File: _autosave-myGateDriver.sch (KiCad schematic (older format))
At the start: 99 parts, among them Q1 BC817, Q10 BC817, Q11 d44vh10, Q12 D45VH10, Q2 BC807, Q3 BC817, Q4 BC817, Q5 BC817, Q6 BUK7880-55A, Q7 BC817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

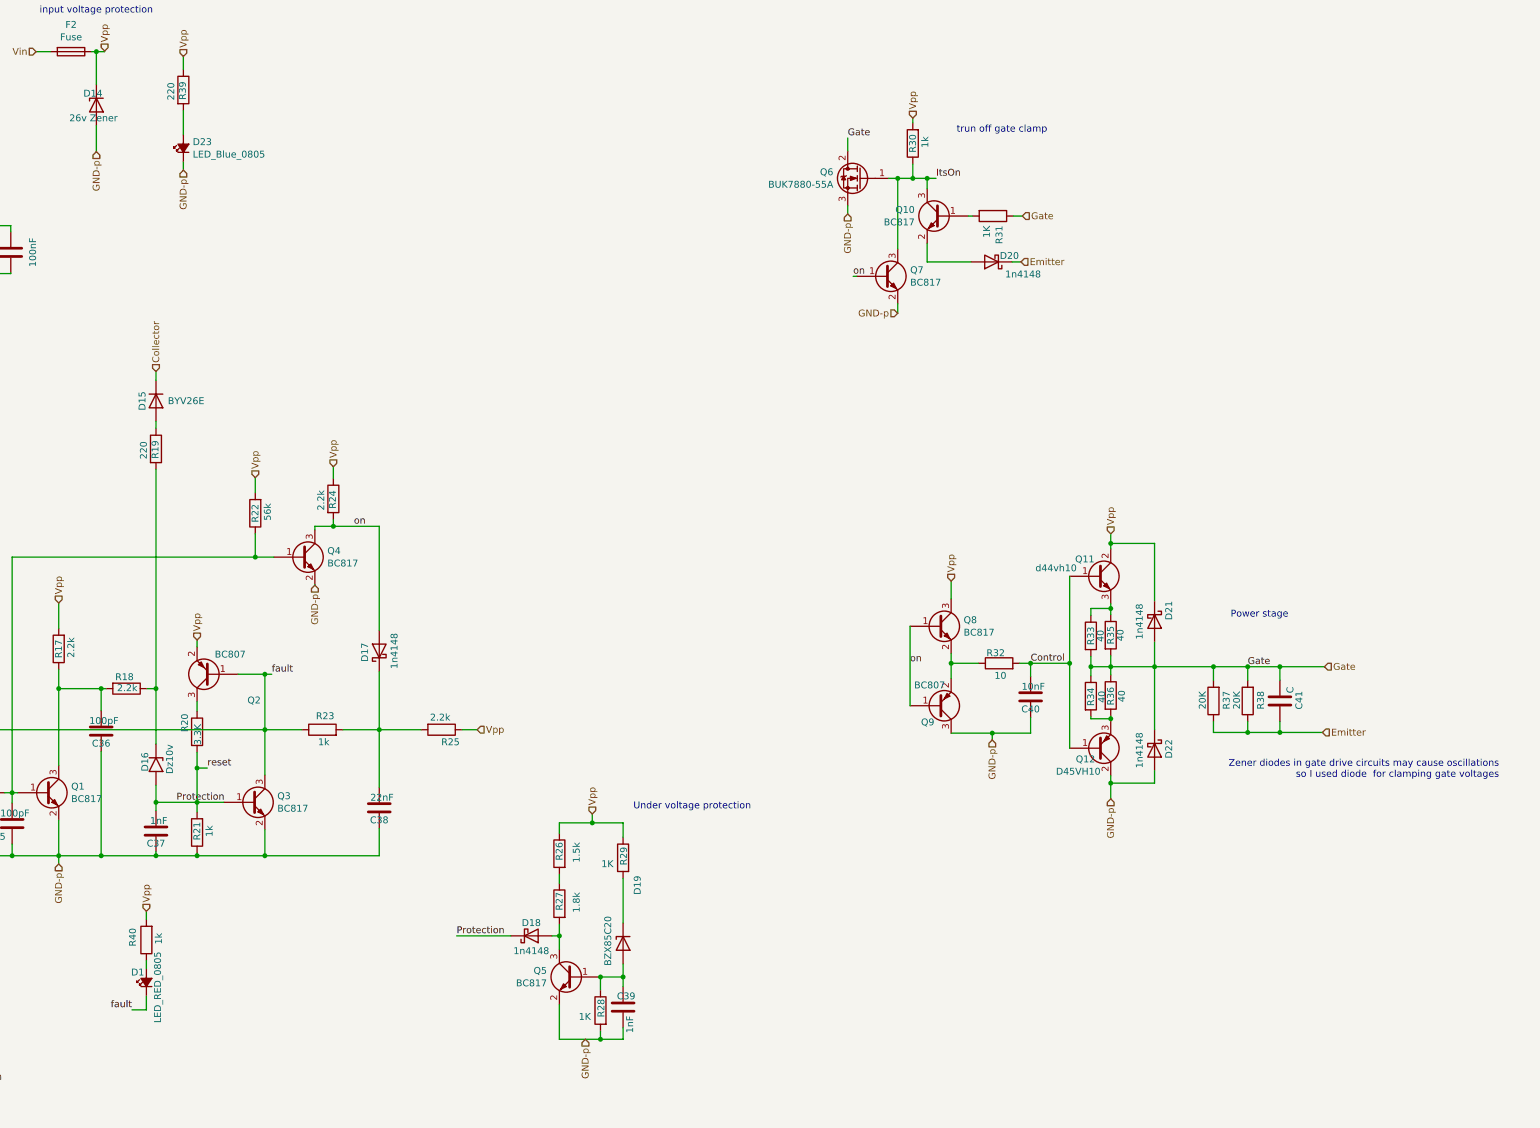
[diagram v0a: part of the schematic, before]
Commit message: soft shutdown wiki pic added
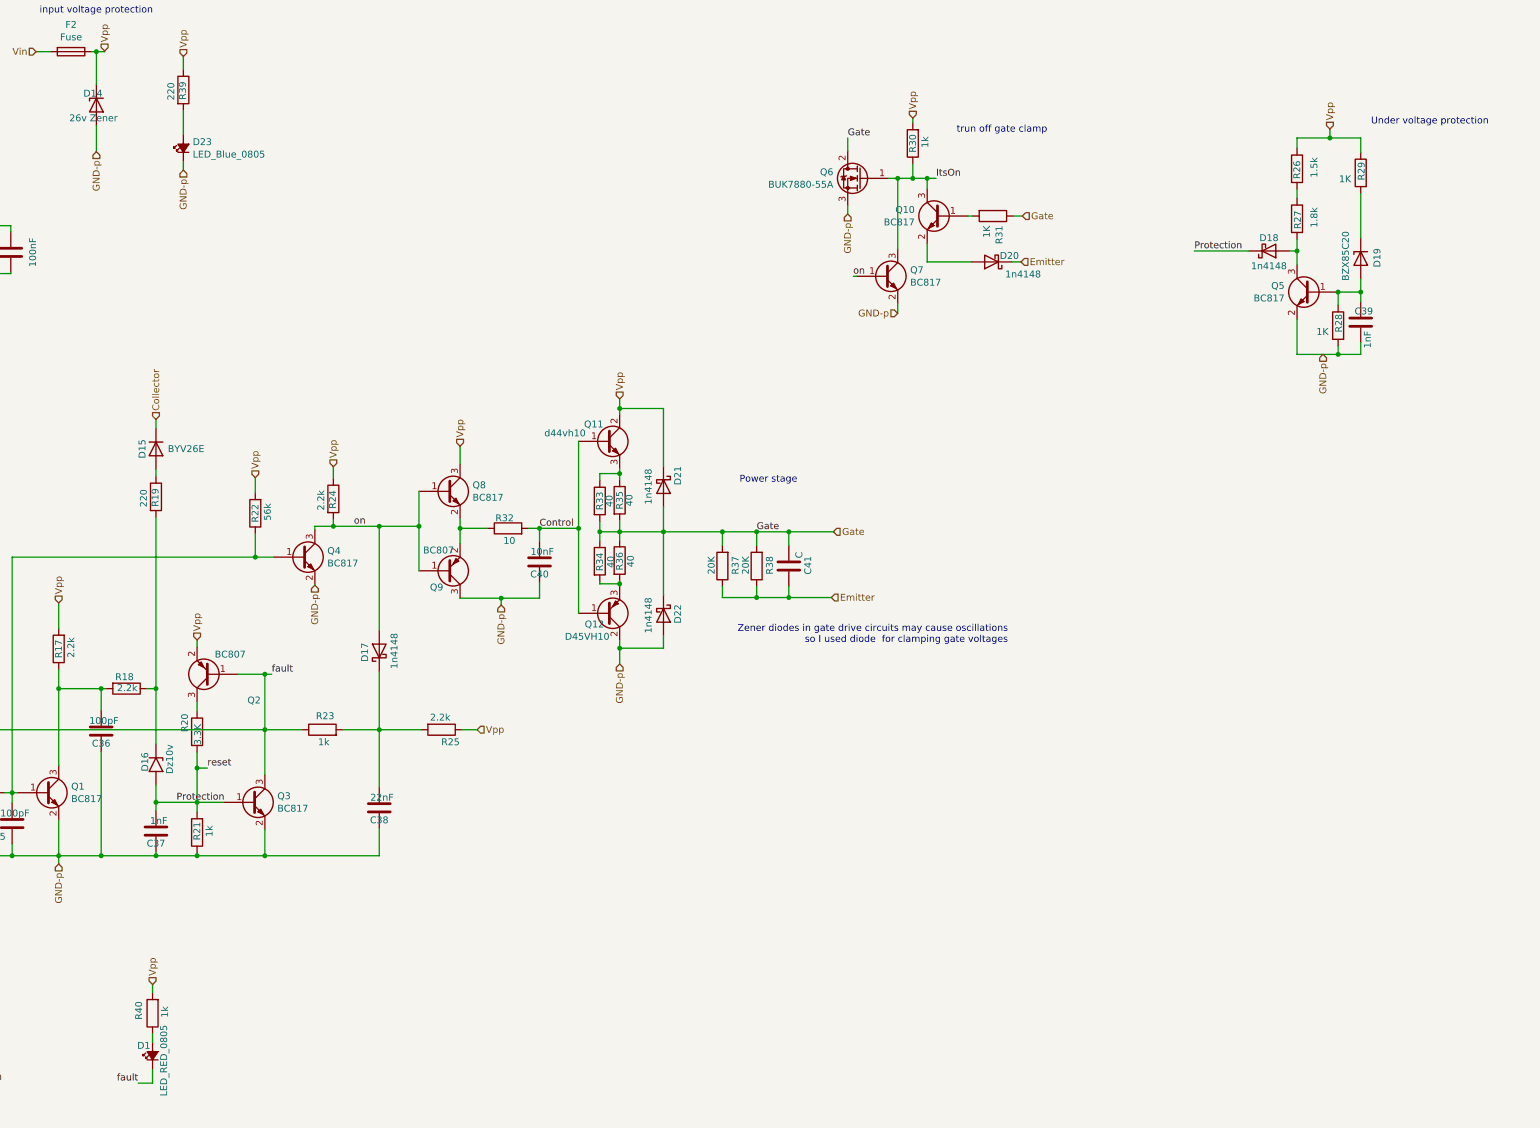
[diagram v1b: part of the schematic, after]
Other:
- moved on the sheet: C39, C40, C41, D1, D15, D18, D19, D21, D22, Q11, Q12, Q5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
